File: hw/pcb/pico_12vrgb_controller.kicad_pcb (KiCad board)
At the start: 2 copper layers, 101 x 31.8 mm, 20 parts, among them J1 Conn_01x04_RGB, J2 Conn_01x04_RGB, J3 Conn_01x04_RGB, J4 Conn_01x04_RGB, J5 Sata_15pin_Power, Q1 DMG2302U, Q10 DMG2302U, Q11 DMG2302U, Q12 DMG2302U, Q2 DMG2302U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

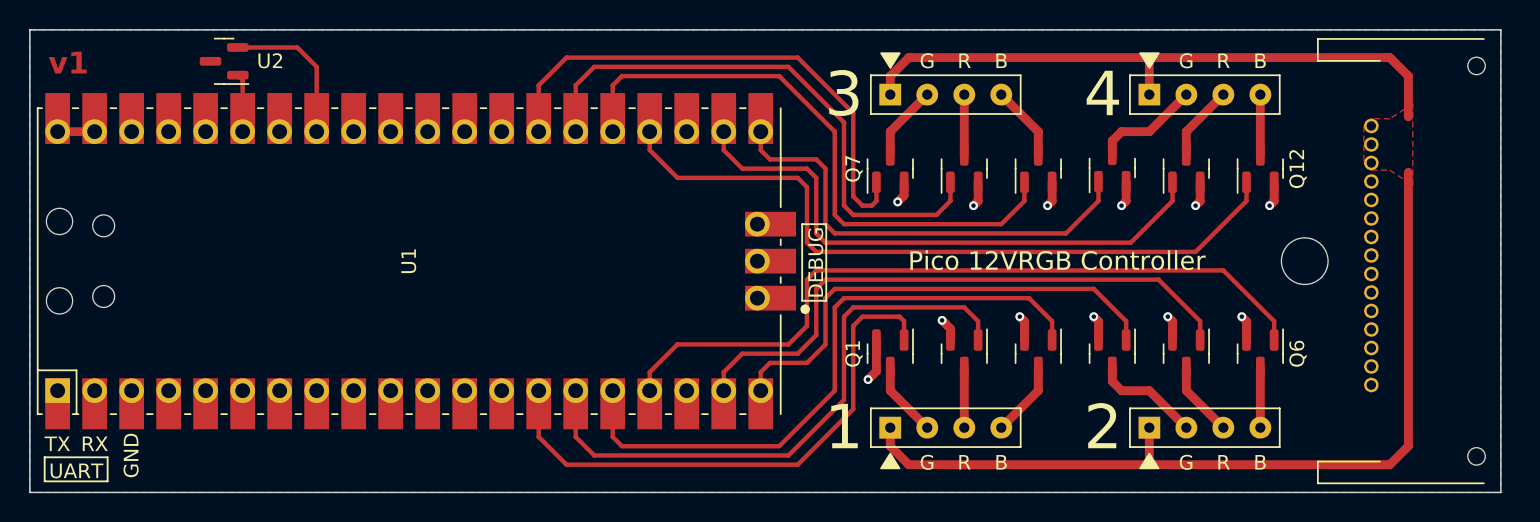
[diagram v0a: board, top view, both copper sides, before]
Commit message: Make PCB exactly 4" x 1.25"
It was 0.025" shorter, which was silly. Make it a bit longer, move the
SATA connector to the same relative position, and change the mounting
hole to be a known distance from the board edge (0.5625")
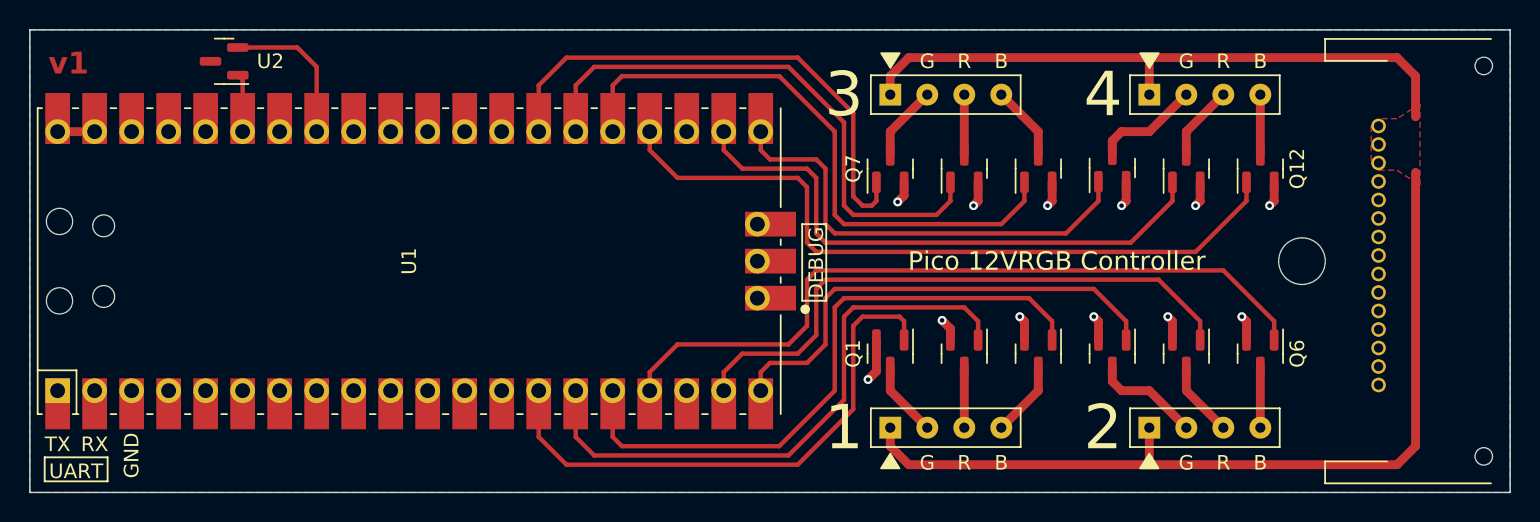
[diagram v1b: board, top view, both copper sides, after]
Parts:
- moved J5 0.50 mm to (163.1, 76.2)
- moved REF** 0.19 mm to (157.8, 76.2)
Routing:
- net +12V: track 102.4 -> 103.4 mm
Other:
- board size 101 x 31.8 mm -> 101.6 x 31.8 mm
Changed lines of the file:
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@@
   )
   (footprint "MountingHole:MountingHole_3.2mm_M3" (layer "F.Cu")
-    (at 157.988 76.2)
+    (at 157.7975 76.2)
     (descr "Mounting Hole 3.2mm, no annular, M3")
     (tags "mounting hole 3.2mm no annular m3")
@@
   )
   (footprint "pico_12vrgb_controller:ModDIY_SATA_15pin_RightAngle_Header" (layer "F.Cu")
-    (at 162.56 76.2 90)
+    (at 163.055 76.2 90)
     (descr "Through hole right-angle 15-pin SATA power connector")
     (property "Sheetfile" "pico_12vrgb_controller.kicad_sch")
@@
   (gr_circle (center 123.698 79.502) (end 123.952 79.502)
     (stroke (width 0.15) (type solid)) (fill solid) (layer "F.SilkS"))
-  (gr_rect (start 70.485 60.325) (end 171.45 92.075)
+  (gr_rect (start 70.485 60.325) (end 172.085 92.075)
     (stroke (width 0.1) (type solid)) (fill none) (layer "Edge.Cuts"))
   (gr_text "v1" (at 71.755 63.5) (layer "F.Cu")
@@
     (effects (font (size 1 1) (thickness 0.15)))
   )
+  (segment (start 164.325 62.23) (end 147.32 62.23) (width 0.6096) (layer "F.Cu") (net 1))
+  (segment (start 147.32 90.17) (end 164.325 90.17) (width 0.6096) (layer "F.Cu") (net 1))
+  (segment (start 164.325 90.17) (end 165.595 88.9) (width 0.6096) (layer "F.Cu") (net 1))
   (segment (start 147.32 87.63) (end 147.32 90.17) (width 0.6096) (layer "F.Cu") (net 1))
   (segment (start 129.54 88.9) (end 130.81 90.17) (width 0.6096) (layer "F.Cu") (net 1))
-  (segment (start 165.1 70.104) (end 165.1 88.9) (width 0.6096) (layer "F.Cu") (net 1))
   (segment (start 129.54 63.5) (end 130.81 62.23) (width 0.6096) (layer "F.Cu") (net 1))
-  (segment (start 147.32 62.23) (end 163.83 62.23) (width 0.6096) (layer "F.Cu") (net 1))
-  (segment (start 165.1 63.5) (end 165.1 66.294) (width 0.6096) (layer "F.Cu") (net 1))
-  (segment (start 163.83 90.17) (end 147.32 90.17) (width 0.6096) (layer "F.Cu") (net 1))
+  (segment (start 165.595 66.294) (end 165.595 63.5) (width 0.6096) (layer "F.Cu") (net 1))
+  (segment (start 165.595 63.5) (end 164.325 62.23) (width 0.6096) (layer "F.Cu") (net 1))
+  (segment (start 165.595 88.9) (end 165.595 70.104) (width 0.6096) (layer "F.Cu") (net 1))
   (segment (start 129.54 87.63) (end 129.54 88.9) (width 0.6096) (layer "F.Cu") (net 1))
   (segment (start 147.32 64.77) (end 147.32 62.23) (width 0.6096) (layer "F.Cu") (net 1))
-  (segment (start 165.1 88.9) (end 163.83 90.17) (width 0.6096) (layer "F.Cu") (net 1))
   (segment (start 130.81 62.23) (end 147.32 62.23) (width 0.6096) (layer "F.Cu") (net 1))
   (segment (start 129.54 64.77) (end 129.54 63.5) (width 0.6096) (layer "F.Cu") (net 1))
   (segment (start 130.81 90.17) (end 147.32 90.17) (width 0.6096) (layer "F.Cu") (net 1))
-  (segment (start 163.83 62.23) (end 165.1 63.5) (width 0.6096) (layer "F.Cu") (net 1))
   (segment (start 129.54 83.4875) (end 129.54 85.09) (width 0.6096) (layer "F.Cu") (net 2))
   (segment (start 129.54 85.09) (end 132.08 87.63) (width 0.6096) (layer "F.Cu") (net 2))
@@
     (polygon
       (pts
-        (xy 163.83 66.421)
-        (xy 162.56 66.421)
-        (xy 162.052 66.929)
-        (xy 162.052 69.469)
-        (xy 162.56 69.957)
-        (xy 163.83 69.957)
-        (xy 165.4048 70.993)
-        (xy 165.4048 65.405)
+        (xy 164.325 66.421)
+        (xy 163.055 66.421)
+        (xy 162.547 66.929)
+        (xy 162.547 69.469)
+        (xy 163.055 69.957)
+        (xy 164.325 69.957)
+        (xy 165.8998 70.993)
+        (xy 165.8998 65.405)
       )
     )
@@
     (polygon
       (pts
-        (xy 171.45 92.075)
+        (xy 172.085 92.075)
         (xy 70.485 92.075)
         (xy 70.485 60.325)
-        (xy 171.45 60.325)
+        (xy 172.085 60.325)
       )
     )
